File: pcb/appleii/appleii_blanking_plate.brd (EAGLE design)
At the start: 75 x 45 mm, 21 parts, among them J1 ATX24RH

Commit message: updated IIGS design
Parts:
- removed C1, C2, C3: (no value), capacitor-wima:C5B2.5
- removed IC1: (no value), v-reg:79XXS
- removed J1: ATX24RH, macse:ATX24_RIGHT_ANGLE
- removed JP1: (no value), pinhead:1X02
- removed JP2: (no value), pinhead:1X03
- removed JP3: (no value), appleii:1X04
- removed U$10, U$11, U$12, U$7, U$8, U$9: EDGEPAD, atx4vc:EDGEPAD
- removed U$6: APPLEII, atx4vc:APPLEII
- U$1: value CAR_FUSE_HOLDER3IN1 -> EDGEPADEDGEPAD_20MM; device atx_power_control:FUSE_HOLDER_3IN1 -> atx4vc:EDGEPAD_20MM
- U$2: value CAR_FUSE_HOLDER3IN1 -> EDGEPAD; device atx_power_control:FUSE_HOLDER_3IN1 -> atx4vc:EDGEPAD
- U$3: value ROCK_SW -> EDGEPAD; device atx4vc:ROCK_SWITCH -> atx4vc:EDGEPAD
- U$4: value M3_MOUNTING_HOLE -> EDGEPAD; device a:M3_MOUNTING_HOLE_PACK -> atx4vc:EDGEPAD
- U$5: value M3_MOUNTING_HOLE -> EDGEPADEDGEPAD_20MM; device a:M3_MOUNTING_HOLE_PACK -> atx4vc:EDGEPAD_20MM
- moved U$3 48.1 mm to (68.6, 10.7), flipped to the bottom, turned to 270 degrees
- moved U$1 39.5 mm to (9.91, 13.5), flipped to the bottom, turned to 270 degrees
- moved U$2 35.9 mm to (66.5, 13.5), flipped to the bottom, turned to 270 degrees
- moved U$13 30.5 mm to (68.6, 13.5), flipped to the bottom
- moved U$5 10.4 mm to (9.91, 10.7), flipped to the bottom, turned to 270 degrees
- moved U$4 9.44 mm to (66.5, 10.7), flipped to the bottom, turned to 270 degrees
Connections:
- removed net +12V: JP2.3, U$2.B0, U$2.B1, U$6.4
- removed net +5V: JP2.1, U$1.A0, U$1.A1, U$6.3
- removed net -12V: IC1.IN, J1.14, U$6.5
- removed net -5V: C3.1, IC1.OUT, U$6.6
- removed net N$1: JP2.2, JP3.2
- removed net N$5: J1.16, JP1.1, U$3.P$2, U$3.P$4
- removed net N$6: C1.1, J1.21, J1.22, J1.23, J1.6, U$1.B0, U$1.B1
- removed net N$8: C2.1, J1.10, J1.11, U$2.A0, U$2.A1
- net GND: now also U$1.P$1, U$2.P$1, U$4.P$1, U$5.P$1; no longer C1.2, C2.2, C3.2, IC1.GND, J1.15, J1.17, J1.18, J1.19, J1.24, J1.3, J1.5, J1.7, JP1.2, JP3.1, U$10.P$1, U$11.P$1, U$12.P$1, U$3.P$3, U$6.1, U$6.2, U$7.P$1, U$8.P$1, U$9.P$1
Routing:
- net N$6: track 92.1 -> 0.00 mm
- net N$8: track 85.8 -> 0.00 mm, vias 1 -> 0
- net +12V: track 52.4 -> 0.00 mm
- net N$5: track 45.3 -> 0.00 mm
- net +5V: track 38.0 -> 0.00 mm
- net -12V: track 31.4 -> 0.00 mm
- net -5V: track 27.4 -> 0.00 mm
- net N$1: track 7.39 -> 0.00 mm
- added copper zone on layer 16, net GND
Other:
- board size 75 x 45 mm -> 72 x 48 mm
- board text added: "12V DC Center Positive"
- board text removed: "+"
- board text removed: "+12"
- board text removed: "+5"
- board text removed: "-12"
- board text removed: "-5"
- board text removed: "12"
- board text removed: "5"
- board text removed: "Apple II / II Plus / IIe PicoPSU Adaptor"
- board text removed: "FUSE 5A MAX"
- board text removed: "G"
- board text removed: "Instructions: picoRC.com"
- board text removed: "PD2 dekuNukem APR23"
- board text removed: "PS_ON"
- board text removed: "min 1uF"

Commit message: cleanup for new run
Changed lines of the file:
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@@
 <?xml version="1.0" encoding="utf-8"?>
 <!DOCTYPE eagle SYSTEM "eagle.dtd">
-<eagle version="9.6.1">
+<eagle version="9.6.2">
 <drawing>
 <settings>
@@
 <signals>
 <signal name="GND">
-<polygon width="0.1524" layer="1" isolate="0.508">
+<polygon width="0.1524" layer="1" isolate="0.6096">
 <vertex x="71" y="48"/>
 <vertex x="-1" y="48"/>
@@
 </polygon>
 <contactref element="U$13" pad="P$1"/>
-<polygon width="0.1524" layer="16">
+<polygon width="0.1524" layer="16" isolate="0.6096">
 <vertex x="-1" y="48"/>
 <vertex x="-1" y="0"/>
@@
 <contactref element="U$4" pad="P$1"/>
 <contactref element="U$5" pad="P$1"/>
+<via x="14.224" y="13.462" extent="1-16" drill="0.6"/>
 </signal>
 </signals>

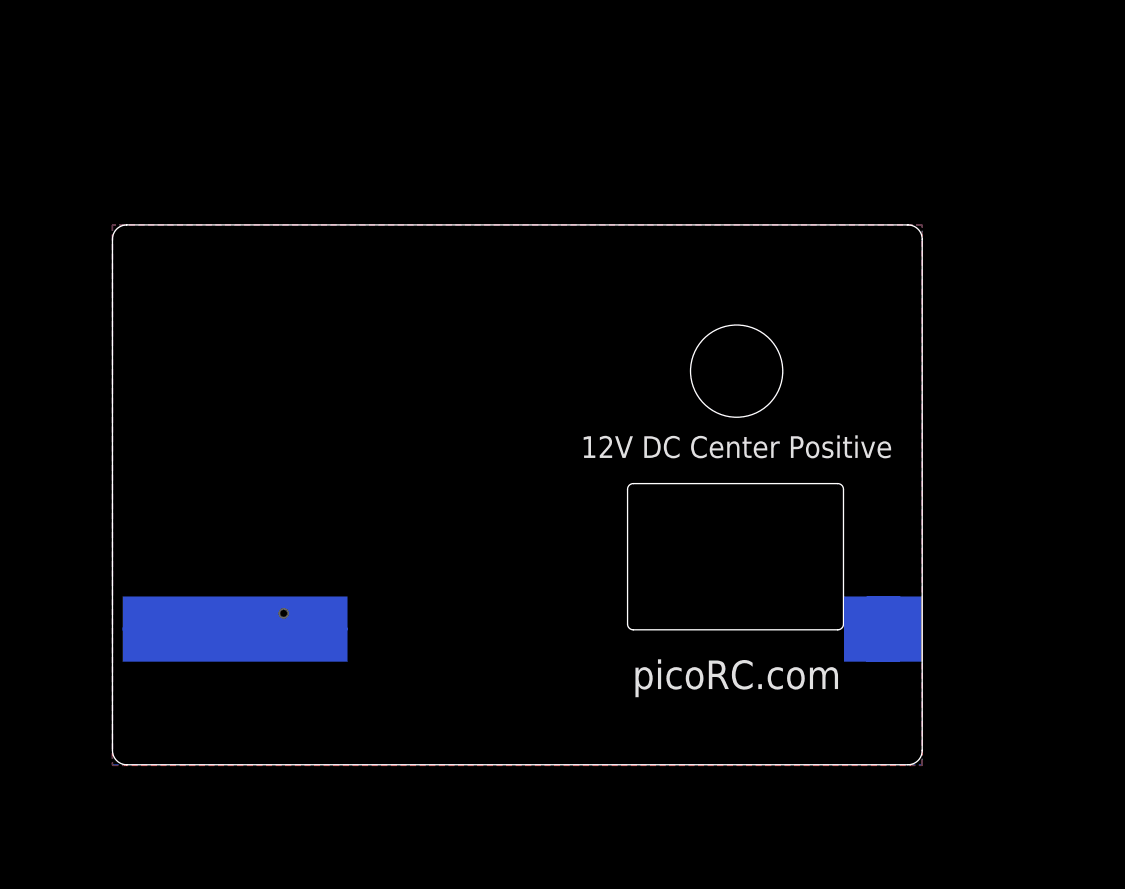
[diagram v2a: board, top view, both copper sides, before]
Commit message: enlarged blanking plate for apple II and II plus
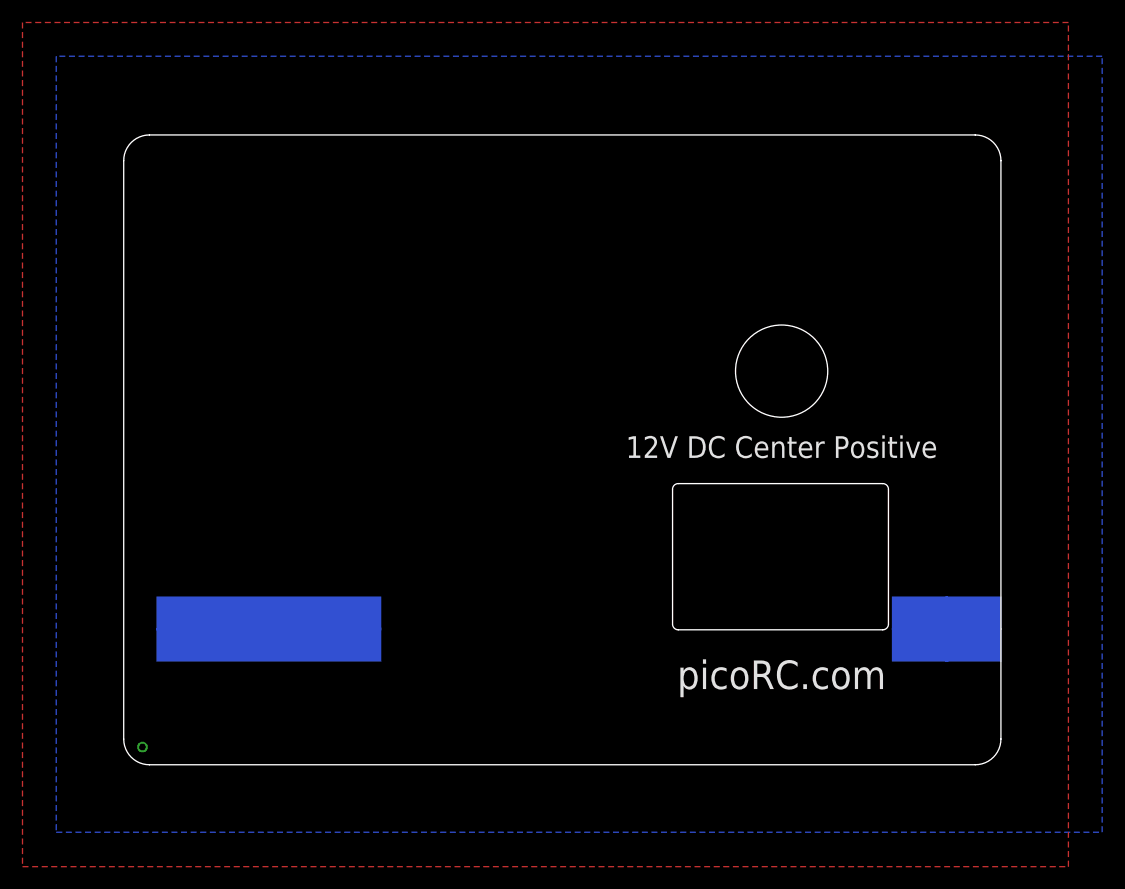
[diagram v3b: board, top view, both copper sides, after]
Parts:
- moved U$13 7.00 mm to (75.6, 13.5)
- moved U$3 7.00 mm to (75.6, 10.7)
- moved U$2 4.25 mm to (70.8, 13.5)
- moved U$4 4.25 mm to (70.8, 10.7)
- moved U$1 3.00 mm to (12.9, 13.5)
- moved U$5 3.00 mm to (12.9, 10.7)
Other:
- board size 72 x 48 mm -> 78 x 56 mm
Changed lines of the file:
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@@
 <setting verticaltext="up"/>
 </settings>
-<grid distance="10" unitdist="mil" unit="mil" style="lines" multiple="1" display="no" altdistance="1" altunitdist="mil" altunit="mil"/>
+<grid distance="5" unitdist="mil" unit="mil" style="lines" multiple="1" display="no" altdistance="1" altunitdist="mil" altunit="mil"/>
 <layers>
 <layer number="1" name="Top" color="4" fill="1" visible="yes" active="yes"/>
@@
 <board>
 <plain>
-<wire x1="71" y1="1.27" x2="71" y2="46.73" width="0" layer="20"/>
-<wire x1="71" y1="46.73" x2="69.73" y2="48" width="0" layer="20" curve="90"/>
-<wire x1="69.73" y1="48" x2="0.27" y2="48" width="0" layer="20"/>
-<wire x1="0.27" y1="48" x2="-1" y2="46.73" width="0" layer="20" curve="90"/>
-<wire x1="-1" y1="46.73" x2="-1" y2="1.27" width="0" layer="20"/>
-<wire x1="-1" y1="1.27" x2="0.27" y2="0" width="0" layer="20" curve="90"/>
-<wire x1="0.27" y1="0" x2="69.73" y2="0" width="0" layer="20"/>
-<wire x1="69.73" y1="0" x2="71" y2="1.27" width="0" layer="20" curve="90"/>
-<text x="54.5" y="28.247" size="1.9304" layer="25" distance="35" align="center">12V DC Center Positive</text>
-<text x="54.5" y="8" size="2.54" layer="25" distance="35" rot="R180" align="center">picoRC.com</text>
-<wire x1="63.492" y1="25" x2="45.308" y2="25" width="0" layer="20"/>
-<wire x1="45.308" y1="25" x2="44.8" y2="24.492" width="0" layer="20" curve="90"/>
-<wire x1="44.8" y1="24.492" x2="44.8" y2="12.508" width="0" layer="20"/>
-<wire x1="44.8" y1="12.508" x2="45.308" y2="12" width="0" layer="20" curve="90"/>
-<wire x1="45.308" y1="12" x2="63.492" y2="12" width="0" layer="20"/>
-<wire x1="63.492" y1="12" x2="64" y2="12.508" width="0" layer="20" curve="90"/>
-<wire x1="64" y1="12.508" x2="64" y2="24.492" width="0" layer="20"/>
-<wire x1="64" y1="24.492" x2="63.492" y2="25" width="0" layer="20" curve="90"/>
-<circle x="54.5" y="35" radius="4.1" width="0.0254" layer="20"/>
+<wire x1="75.714" y1="56" x2="2.286" y2="56" width="0" layer="20"/>
+<wire x1="2.286" y1="56" x2="0" y2="53.714" width="0" layer="20" curve="90"/>
+<wire x1="0" y1="53.714" x2="0" y2="2.286" width="0" layer="20"/>
+<wire x1="0" y1="2.286" x2="2.286" y2="0" width="0" layer="20" curve="90"/>
+<wire x1="2.286" y1="0" x2="75.714" y2="0" width="0" layer="20"/>
+<wire x1="75.714" y1="0" x2="78" y2="2.286" width="0" layer="20" curve="90"/>
+<wire x1="78" y1="2.286" x2="78" y2="53.714" width="0" layer="20"/>
+<wire x1="78" y1="53.714" x2="75.714" y2="56" width="0" layer="20" curve="90"/>
+<text x="58.5" y="28.247" size="1.9304" layer="25" distance="35" align="center">12V DC Center Positive</text>
+<text x="58.5" y="8" size="2.54" layer="25" distance="35" rot="R180" align="center">picoRC.com</text>
+<wire x1="67.492" y1="25" x2="49.308" y2="25" width="0" layer="20"/>
+<wire x1="49.308" y1="25" x2="48.8" y2="24.492" width="0" layer="20" curve="90"/>
+<wire x1="48.8" y1="24.492" x2="48.8" y2="12.508" width="0" layer="20"/>
+<wire x1="48.8" y1="12.508" x2="49.308" y2="12" width="0" layer="20" curve="90"/>
+<wire x1="49.308" y1="12" x2="67.492" y2="12" width="0" layer="20"/>
+<wire x1="67.492" y1="12" x2="68" y2="12.508" width="0" layer="20" curve="90"/>
+<wire x1="68" y1="12.508" x2="68" y2="24.492" width="0" layer="20"/>
+<wire x1="68" y1="24.492" x2="67.492" y2="25" width="0" layer="20" curve="90"/>
+<circle x="58.5" y="35" radius="4.1" width="0.0254" layer="20"/>
 </plain>
 <attributes>
@@
 </autorouter>
 <elements>
-<element name="U$13" library="atx4vc" package="EDGEPAD" value="EDGEPAD" x="68.564" y="13.462" smashed="yes" rot="MR90"/>
-<element name="U$1" library="atx4vc" package="EDGEPAD_20MM" value="EDGEPADEDGEPAD_20MM" x="9.906" y="13.462" smashed="yes" rot="MR270"/>
-<element name="U$2" library="atx4vc" package="EDGEPAD" value="EDGEPAD" x="66.548" y="13.462" smashed="yes" rot="MR270"/>
-<element name="U$3" library="atx4vc" package="EDGEPAD" value="EDGEPAD" x="68.564" y="10.668" smashed="yes" rot="MR270"/>
-<element name="U$4" library="atx4vc" package="EDGEPAD" value="EDGEPAD" x="66.548" y="10.668" smashed="yes" rot="MR270"/>
-<element name="U$5" library="atx4vc" package="EDGEPAD_20MM" value="EDGEPADEDGEPAD_20MM" x="9.906" y="10.668" smashed="yes" rot="MR270"/>
+<element name="U$13" library="atx4vc" package="EDGEPAD" value="EDGEPAD" x="75.564" y="13.462" smashed="yes" rot="MR90"/>
+<element name="U$1" library="atx4vc" package="EDGEPAD_20MM" value="EDGEPADEDGEPAD_20MM" x="12.906" y="13.462" smashed="yes" rot="MR270"/>
+<element name="U$2" library="atx4vc" package="EDGEPAD" value="EDGEPAD" x="70.802" y="13.462" smashed="yes" rot="MR270"/>
+<element name="U$3" library="atx4vc" package="EDGEPAD" value="EDGEPAD" x="75.564" y="10.668" smashed="yes" rot="MR270"/>
+<element name="U$4" library="atx4vc" package="EDGEPAD" value="EDGEPAD" x="70.802" y="10.668" smashed="yes" rot="MR270"/>
+<element name="U$5" library="atx4vc" package="EDGEPAD_20MM" value="EDGEPADEDGEPAD_20MM" x="12.906" y="10.668" smashed="yes" rot="MR270"/>
 </elements>
 <signals>
 <signal name="GND">
 <polygon width="0.1524" layer="1" isolate="0.6096">
-<vertex x="71" y="48"/>
-<vertex x="-1" y="48"/>
-<vertex x="-1" y="-0.062"/>
-<vertex x="71" y="-0.062"/>
+<vertex x="84" y="66"/>
+<vertex x="-9" y="66"/>
+<vertex x="-9" y="-9.062"/>
+<vertex x="84" y="-9.062"/>
 </polygon>
 <contactref element="U$13" pad="P$1"/>
 <polygon width="0.1524" layer="16" isolate="0.6096">
-<vertex x="-1" y="48"/>
-<vertex x="-1" y="0"/>
-<vertex x="71" y="0"/>
-<vertex x="71" y="48"/>
+<vertex x="-6" y="63"/>
+<vertex x="-6" y="-6"/>
+<vertex x="87" y="-6"/>
+<vertex x="87" y="63"/>
 </polygon>
 <contactref element="U$1" pad="P$1"/>
@@
 <contactref element="U$4" pad="P$1"/>
 <contactref element="U$5" pad="P$1"/>
-<via x="14.224" y="13.462" extent="1-16" drill="0.6"/>
+<via x="1.668" y="1.572" extent="1-16" drill="0.6"/>
 </signal>
 </signals>
@@
 <mfgpreviewcolor name="substratecolor" color="0xFF786E46"/>
 </mfgpreviewcolors>
+<errors>
+</errors>
 </board>
 </drawing>
